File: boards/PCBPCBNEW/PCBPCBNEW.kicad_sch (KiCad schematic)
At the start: 74 parts, among them J1 Screw_Terminal_01x02, J4 Screw_Terminal_01x06, U1 SIC431AED-T1-GE3, U2 SIC431AED-T1-GE3, U3 SIC431AED-T1-GE3

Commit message: GL
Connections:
- removed net GL: U1.10 (GL), U1.11 (GL), U1.28 (GL), U2.10 (GL), U2.11 (GL), U2.28 (GL), U3.10 (GL), U3.11 (GL), U3.28 (GL)
- new net: U1.10 (GL), U1.11 (GL), U1.28 (GL)
- new net: U3.10 (GL), U3.11 (GL), U3.28 (GL)
- new net: U2.10 (GL), U2.11 (GL), U2.28 (GL)
- no-connect marks 0 -> 3
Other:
- moved on the sheet: U1, U2

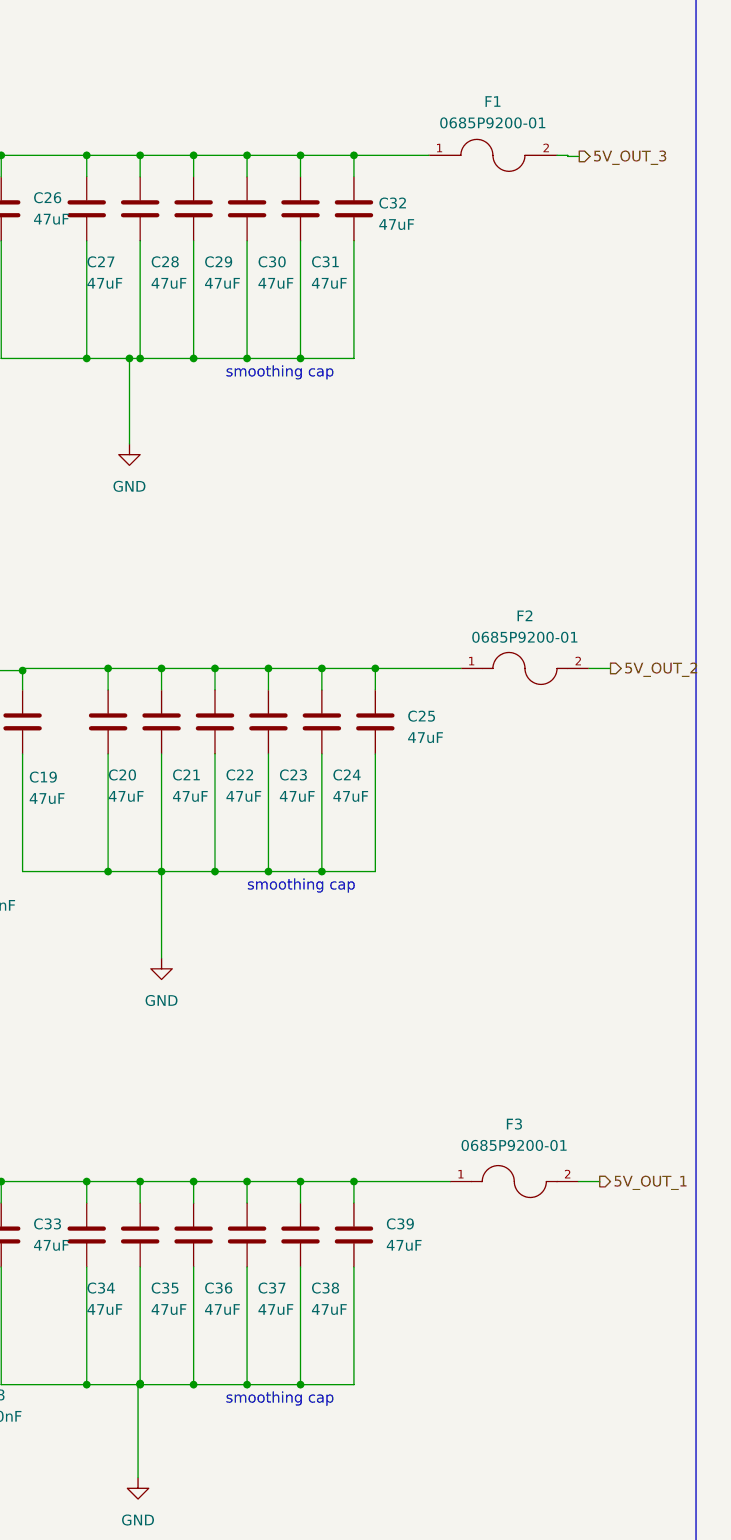
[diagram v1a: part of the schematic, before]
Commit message: Changed capacitors
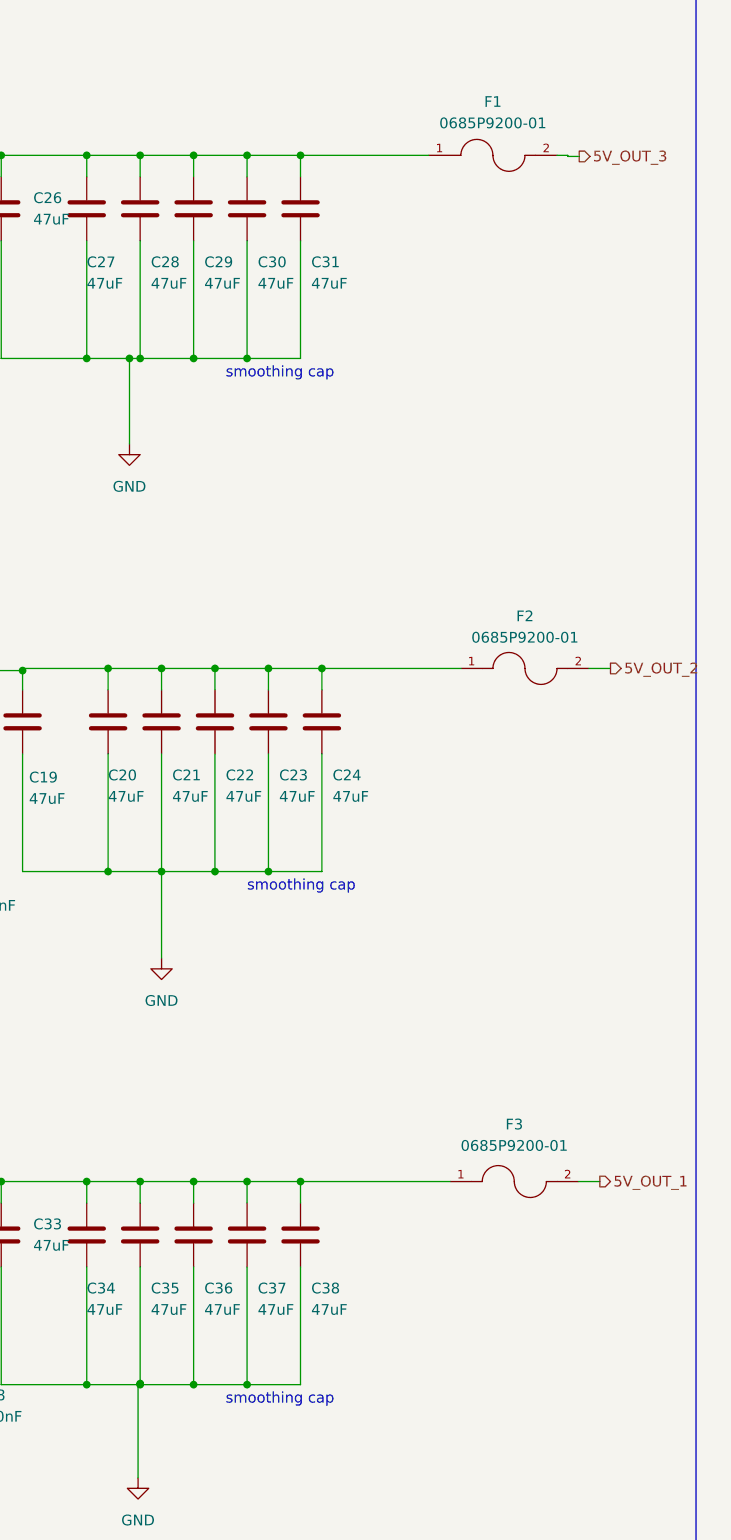
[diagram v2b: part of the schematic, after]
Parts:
- removed C25, C32, C39: 47uF, Capacitor_SMD:C_0805_2012Metric, symbol Device:C

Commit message: pcbpcbnew2
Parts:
- added C25, C44, C48: 100nF, Capacitor_SMD:C_0805_2012Metric, symbol Device:C
- added C32, C39, C40, C41, C42, C43: 47uF, Capacitor_SMD:C_0805_2012Metric, symbol Device:C
- added C45: 1uF, Capacitor_SMD:C_0805_2012Metric, symbol Device:C
- added C46: 4.7uF, Capacitor_SMD:C_0805_2012Metric, symbol Device:C
- added C47: 150uF, Capacitor_THT:CP_Radial_D12.5mm_P5.00mm, symbol Device:C_Polarized_Small_US
- added F4: 0685P9200-01, IRIS:FUSC3215X83N, symbol IRIS:0685P9200-01
- added L4: 1.2uH, Inductor_SMD:L_Vishay_IHLP-5050, symbol Device:L
- added R25: 3.3, Resistor_SMD:R_0805_2012Metric, symbol Device:R_Small_US
- added R26: 10k, Resistor_SMD:R_0805_2012Metric, symbol Device:R_Small_US
- added R27: 73.2, Resistor_SMD:R_0805_2012Metric, symbol Device:R_Small_US
- added R28, R29: 100k, Resistor_SMD:R_0805_2012Metric, symbol Device:R_Small_US
- added R30: 200k, Resistor_SMD:R_0805_2012Metric, symbol Device:R_Small_US
- added R31: 562k, Resistor_SMD:R_0805_2012Metric, symbol Device:R_Small_US
- added R32: 309k, Resistor_SMD:R_0805_2012Metric, symbol Device:R_Small_US
- added U4: SIC431AED-T1-GE3, SIC431AED_T1_GE3:REGULATOR_SIC431AED-T1-GE3, symbol SIC431AED-T1-GE3:SIC431AED-T1-GE3
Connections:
- net 5V_OUT_3: now also F4.2
- net GND: now also C32.2, C39.2, C40.2, C41.2, C42.2, C43.2, C44.2, C45.2, C46.2, C47.2, C48.2, R26.2, R30.1, R32.2, U4.13 (PGND__2), U4.16 (AGND), U4.25 (AGND__1), U4.27_1 (PGND__3), U4.27_2 (PGND__4), U4.3 (PGND), U4.4 (PGND__1)
- net V_BAT_IN: now also C47.1, C48.1, R31.1, U4.1 (VIN)
- new net: C32.1, C39.1, C40.1, C41.1, C42.1, C43.1, C44.1, F4.1, L4.2, R27.2, U4.18 (VOUT)
- new net: C46.1, U4.12 (VDRV)
- new net: R26.1, R27.1, U4.17 (FB)
- new net: R31.2, R32.1, U4.19 (EN)
- new net: C45.1, R28.1, R29.1, U4.15 (VDD)
- new net: C25.1, R25.2
- new net: C25.2, U4.23 (BOOT)
- new net: L4.1, U4.5 (SW)
- new net: R29.2, U4.14 (PGOOD)
- new net: R25.1, U4.24 (PHASE)
- new net: R30.2, U4.20 (MODE2)
- new net: R28.2, U4.21 (MODE1)
- no-connect marks 3 -> 6
